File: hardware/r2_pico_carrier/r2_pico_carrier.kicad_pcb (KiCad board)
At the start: 2 copper layers, 80 x 72 mm, 63 parts, among them J1 5V in, J2 OLED SSD1306, SW1 display, U1 PCA9517A

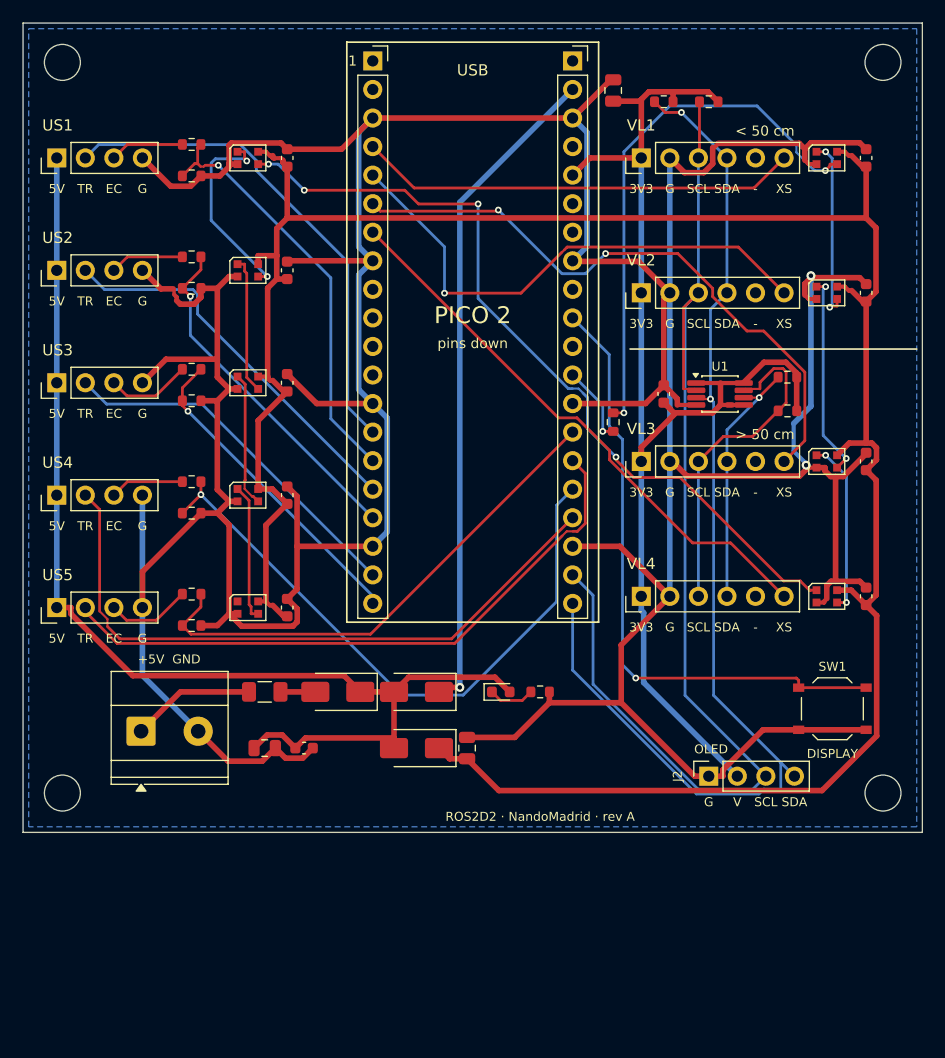
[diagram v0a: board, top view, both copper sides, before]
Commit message: Carrier board: PCA9517A port A (no offset) on the long cables; README warns about Pico orientation, terminal wiring with USB in, SW1 rotation
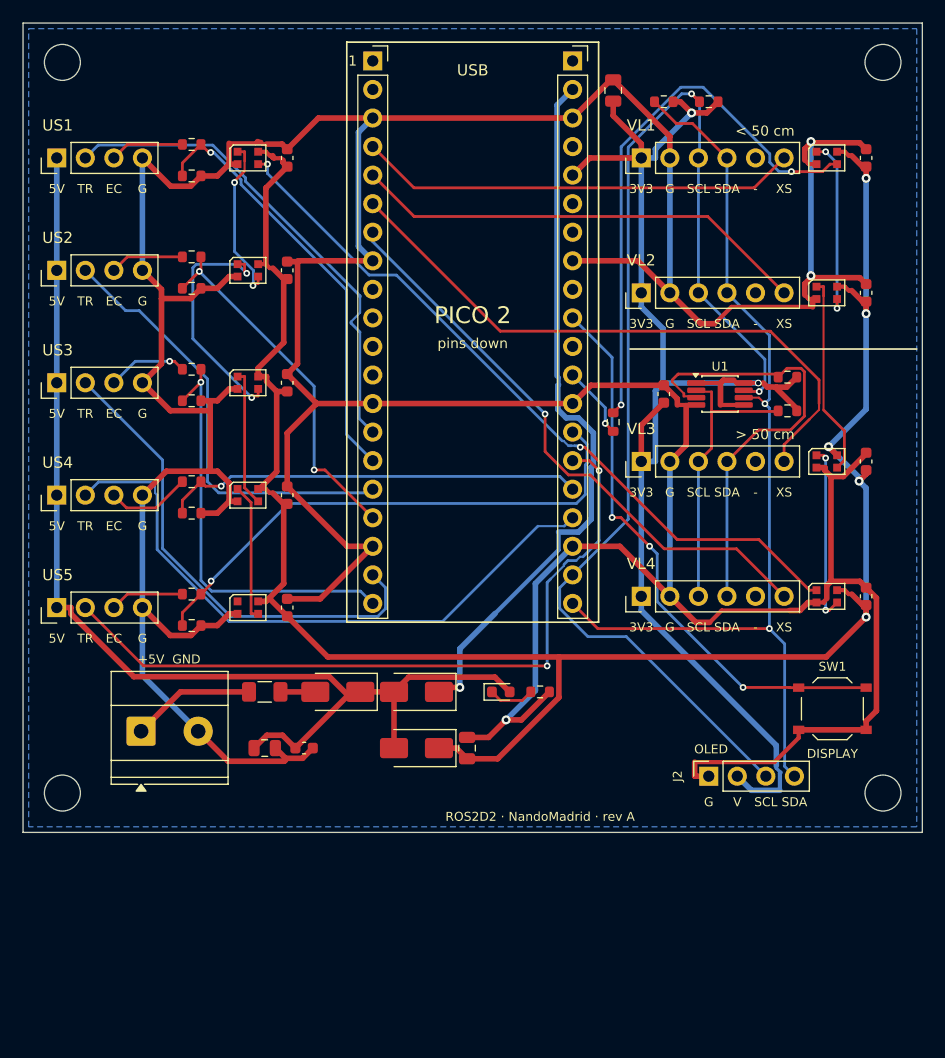
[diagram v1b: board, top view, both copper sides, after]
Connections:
- U1 pad 2: SCL -> SCL_L
- U1 pad 3: SDA -> SDA_L
- U1 pad 6: SDA_L -> SDA
- U1 pad 7: SCL_L -> SCL
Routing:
- net VLED: track 214.8 -> 181.8 mm, vias 0 -> 5
- net ECHO4_P: track 56.5 -> 37.5 mm
- net SDA_L: track 22.8 -> 40.1 mm, vias 1 -> 0
- net GND: track 470.4 -> 453.2 mm, vias 2 -> 3
- net +3V3: track 110.1 -> 124.0 mm, vias 0 -> 2
- net SDA: track 100.1 -> 86.9 mm
- net TRIG3: track 32.6 -> 43.7 mm
- net LED_D6: track 12.2 -> 21.8 mm, vias 0 -> 2
- net TRIG5: track 56.5 -> 65.8 mm, vias 0 -> 2
- net ECHO3_P: track 28.5 -> 37.2 mm
- net LED_D4: track 72.1 -> 65.9 mm, vias 4 -> 2
- net XSHUT2: track 46.7 -> 40.9 mm, vias 1 -> 0
- net BTN: track 55.6 -> 50.6 mm, vias 1 -> 3
- net TRIG2: track 34.7 -> 39.3 mm
- net VSYS: track 59.4 -> 63.8 mm
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
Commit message: Carrier board: OLED (HS96L03W2C03) fitted at the factory, lying flat; round Astromech Spain logo; 80 x 90 mm
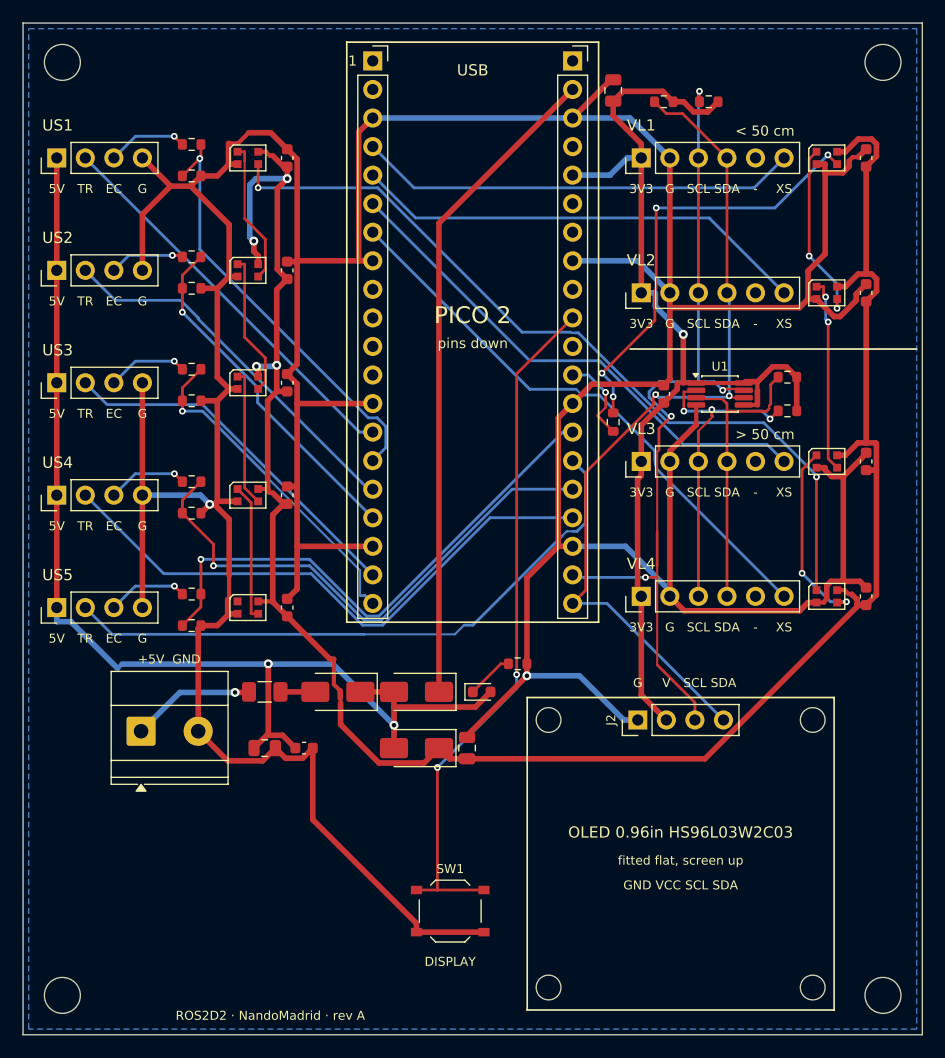
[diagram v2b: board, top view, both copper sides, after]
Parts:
- added H5: M2 OLED, MountingHole:MountingHole_2.2mm_M2, F.Cu at (46.8, 62.0)
- added H6: M2 OLED, MountingHole:MountingHole_2.2mm_M2, F.Cu at (70.2, 62.0)
- added H7: M2 OLED, MountingHole:MountingHole_2.2mm_M2, F.Cu at (46.8, 85.8)
- added H8: M2 OLED, MountingHole:MountingHole_2.2mm_M2, F.Cu at (70.2, 85.8)
- J2: value OLED SSD1306 -> OLED HS96L03W2C03; footprint Connector_PinSocket_2.54mm:PinSocket_1x04_P2.54mm_Vertical -> Connector_PinHeader_2.54mm:PinHeader_1x04_P2.54mm_Vertical
- moved SW1 38.5 mm to (38.0, 79.0)
- moved H3 18.0 mm to (3.50, 86.5)
- moved H4 18.0 mm to (76.5, 86.5)
- moved J2 8.05 mm to (54.7, 62.0)
- moved R1 3.20 mm to (44.0, 57.0)
- moved D4 1.70 mm to (40.8, 59.5)
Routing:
- net SCL: track 107.6 -> 75.7 mm, vias 2 -> 4
- net +3V3: track 124.0 -> 96.4 mm, vias 2 -> 1
- net SDA_L: track 40.1 -> 27.1 mm
- net BTN: track 50.6 -> 61.9 mm, vias 3 -> 2
- net TRIG3: track 43.7 -> 32.6 mm
- net ECHO4_P: track 37.5 -> 48.1 mm
- net TRIG5: track 65.8 -> 55.6 mm, vias 2 -> 0
- net LED_DIN: track 49.2 -> 39.0 mm, vias 2 -> 4
- net SDA: track 86.9 -> 77.2 mm
- net LED_D6: track 21.8 -> 12.8 mm, vias 2 -> 0
- net XSHUT3: track 54.7 -> 46.1 mm
- net TRIG1: track 44.0 -> 35.7 mm
- net ECHO3_P: track 37.2 -> 29.8 mm
- net LED_D4: track 65.9 -> 72.6 mm
- net VLED: track 181.8 -> 187.6 mm, vias 5 -> 4
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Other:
- board size 80 x 72 mm -> 80 x 90 mm
- board text added: "GND VCC SCL SDA"
- board text added: "OLED 0.96in HS96L03W2C03"
- board text added: "by NandoMadrid"
- board text added: "fitted flat, screen up"
- board text removed: "OLED"
- board text removed: "ROS2D2 · by NandoMadrid"

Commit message: Carrier board: in-stock Pico sockets (C2905423) and power LED (C2286, red); OLED plugs into a 4-pin socket (C2718488)
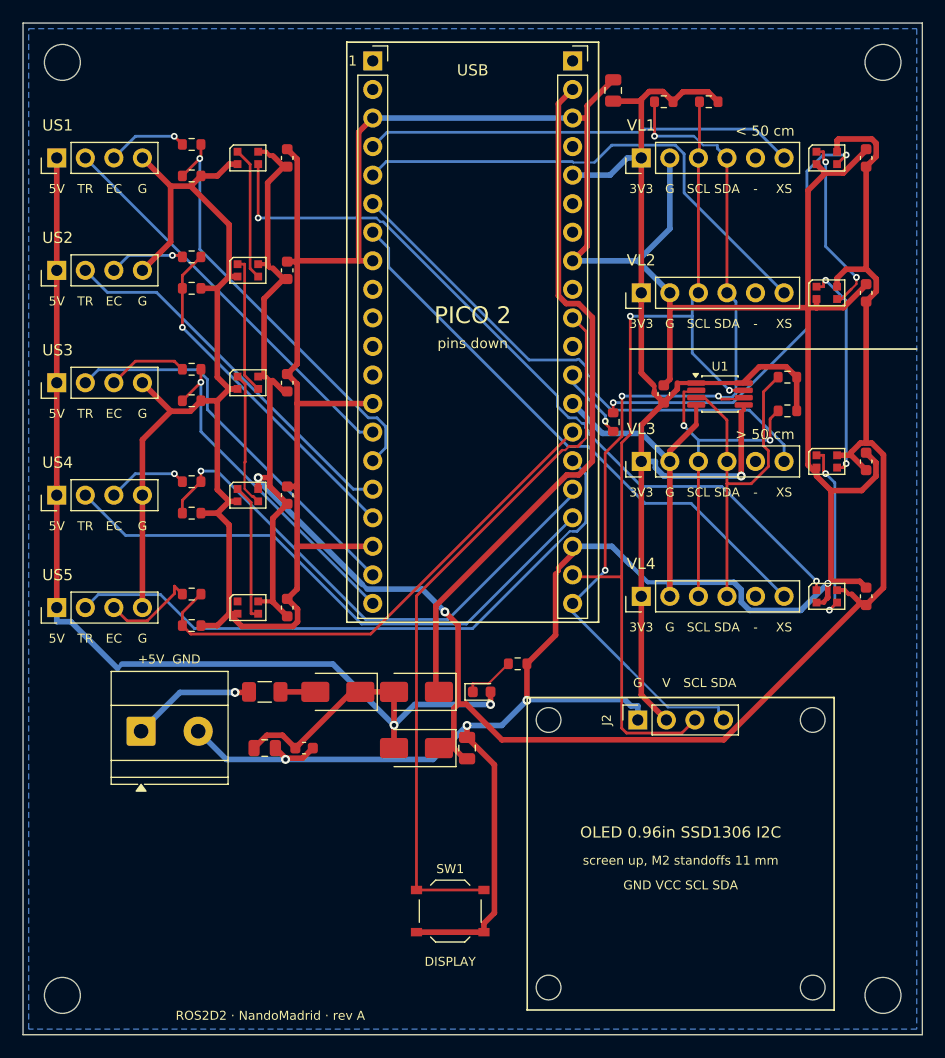
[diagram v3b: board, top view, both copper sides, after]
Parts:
- D4: value green -> red
- J2: value OLED HS96L03W2C03 -> OLED socket; footprint Connector_PinHeader_2.54mm:PinHeader_1x04_P2.54mm_Vertical -> Connector_PinSocket_2.54mm:PinSocket_1x04_P2.54mm_Vertical
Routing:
- net GND: track 451.6 -> 469.7 mm, vias 2 -> 4
- net +3V3: track 96.4 -> 108.3 mm
- net SCL: track 75.7 -> 82.7 mm, vias 4 -> 2
- net VLED: track 187.6 -> 194.1 mm, vias 4 -> 2
- net SDA: track 77.2 -> 83.3 mm, vias 2 -> 4
- net SDA_L: track 27.1 -> 32.2 mm
- net XSHUT2: track 40.9 -> 45.2 mm
- net VSYS: track 58.5 -> 62.5 mm
- net LED_D4: track 72.6 -> 69.5 mm
- net +5V: track 103.5 -> 106.3 mm
- net ECHO5_P: track 48.5 -> 46.0 mm, vias 1 -> 0
- net TRIG3: track 32.6 -> 35.2 mm
- net BTN: track 61.9 -> 64.3 mm, vias 2 -> 0
- net LED_D2: track 17.2 -> 19.4 mm
- net XSHUT3: track 46.1 -> 48.0 mm
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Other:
- board text added: "OLED 0.96in SSD1306 I2C"
- board text added: "screen up, M2 standoffs 11 mm"
- board text removed: "OLED 0.96in HS96L03W2C03"
- board text removed: "fitted flat, screen up"

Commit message: Carrier board: WS2812B-2020-V6 (in stock) for the diagnostic LEDs
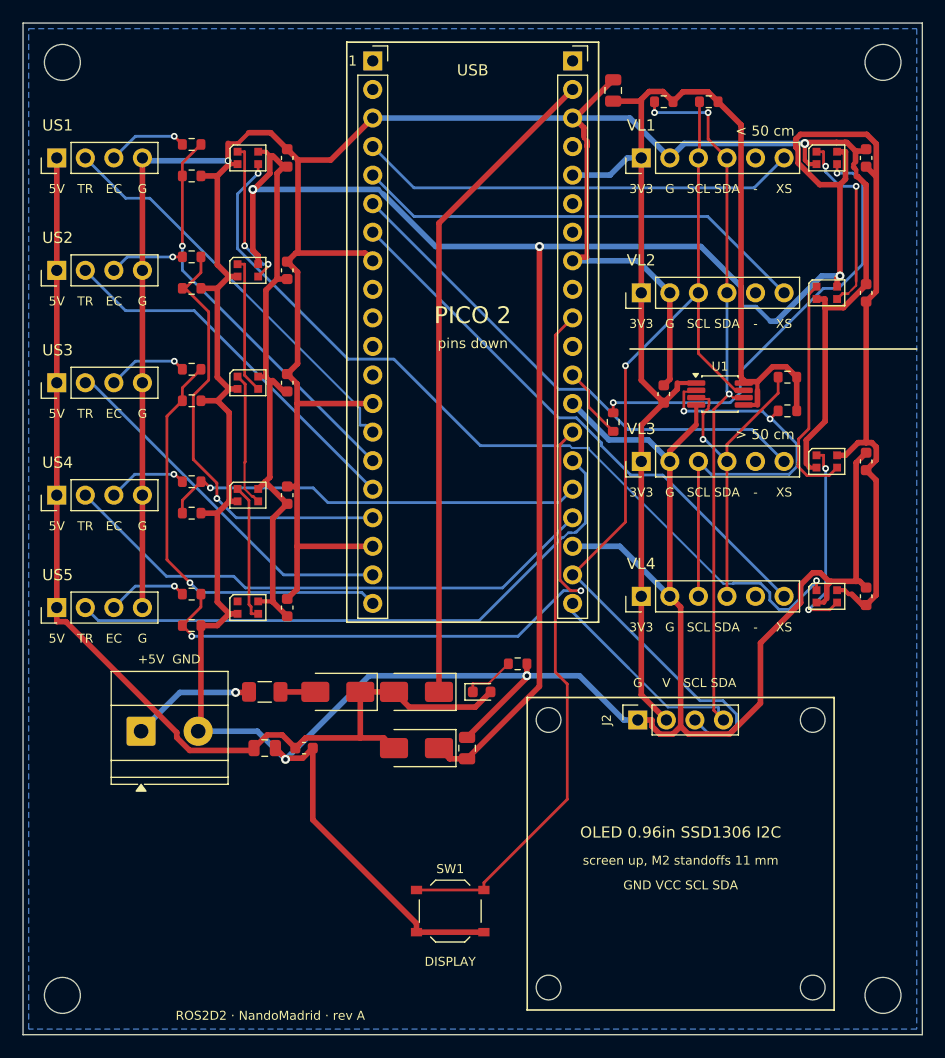
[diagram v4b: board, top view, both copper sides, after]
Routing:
- net VLED: track 194.1 -> 251.3 mm, vias 2 -> 3
- net GND: track 469.7 -> 496.2 mm
- net +5V: track 106.3 -> 94.9 mm, vias 2 -> 0
- net ECHO5_P: track 46.0 -> 57.0 mm, vias 0 -> 2
- net ECHO4_P: track 48.1 -> 37.8 mm
- net SCL_L: track 29.2 -> 38.7 mm
- net +3V3: track 108.3 -> 117.1 mm, vias 1 -> 0
- net ECHO3_P: track 29.5 -> 38.1 mm
- net ECHO2_P: track 30.9 -> 39.2 mm
- net LED_D4: track 69.5 -> 75.5 mm
- net XSHUT2: track 45.2 -> 40.9 mm
- net VSYS: track 62.5 -> 58.5 mm
- net BTN: track 64.3 -> 61.0 mm
- net SDA_L: track 32.2 -> 29.3 mm, vias 0 -> 1
- net TRIG4: track 52.0 -> 49.4 mm
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
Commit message: Carrier board: classic 5050 WS2812B (C2874885) for the diagnostic LEDs
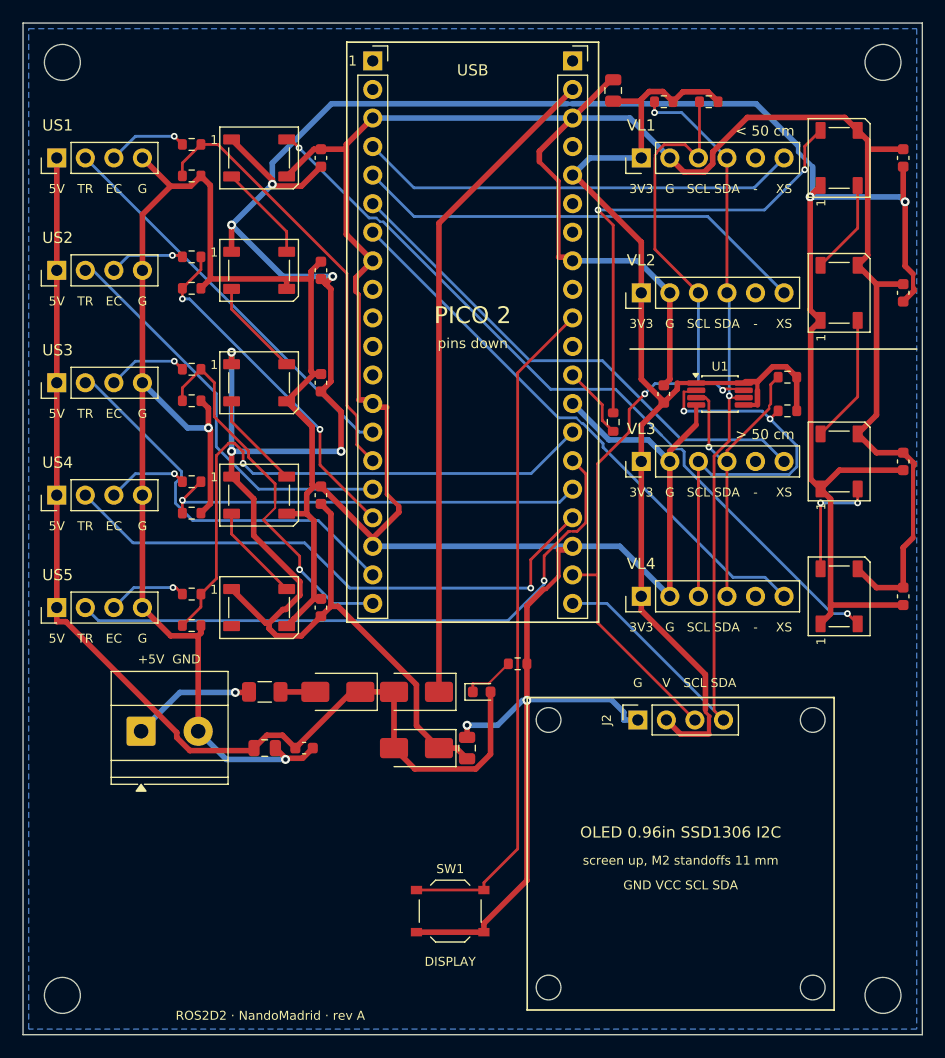
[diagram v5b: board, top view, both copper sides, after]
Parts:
- LED1, LED2, LED3, LED4, LED5, LED6, LED7, LED8, LED9: value WS2812B-2020 -> WS2812B; footprint LED_SMD:LED_WS2812B-2020_PLCC4_2.0x2.0mm -> LED_SMD:LED_WS2812B_PLCC4_5.0x5.0mm_P3.2mm
- moved C11 3.30 mm to (78.3, 12.0)
- moved C12 3.30 mm to (78.3, 24.0)
- moved C13 3.30 mm to (78.3, 39.0)
- moved C14 3.30 mm to (78.3, 51.0)
- moved C15 3.00 mm to (26.5, 12.0)
- moved C16 3.00 mm to (26.5, 22.0)
- moved C17 3.00 mm to (26.5, 32.0)
- moved C18 3.00 mm to (26.5, 42.0)
- moved C19 3.00 mm to (26.5, 52.0)
- moved LED1 1.10 mm to (72.6, 12.0), turned to 90 degrees
- moved LED2 1.10 mm to (72.6, 24.0), turned to 90 degrees
- moved LED3 1.10 mm to (72.6, 39.0), turned to 90 degrees
- moved LED4 1.10 mm to (72.6, 51.0), turned to 90 degrees
- moved LED5 1.00 mm to (21.0, 12.0)
- moved LED6 1.00 mm to (21.0, 22.0)
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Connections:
- LED1 pad 1: LED_D1 -> VLED
- LED1 pad 2: GND -> LED_D1
- LED1 pad 3: LED_DIN -> GND
- LED1 pad 4: VLED -> LED_DIN
- LED2 pad 1: LED_D2 -> VLED
- LED2 pad 2: GND -> LED_D2
- LED2 pad 3: LED_D1 -> GND
- LED2 pad 4: VLED -> LED_D1
- LED3 pad 1: LED_D3 -> VLED
- LED3 pad 2: GND -> LED_D3
- LED3 pad 3: LED_D2 -> GND
- LED3 pad 4: VLED -> LED_D2
- LED4 pad 1: LED_D4 -> VLED
- LED4 pad 2: GND -> LED_D4
- LED4 pad 3: LED_D3 -> GND
- LED4 pad 4: VLED -> LED_D3
- LED5 pad 1: LED_D5 -> VLED
- LED5 pad 2: GND -> LED_D5
- LED5 pad 3: LED_D4 -> GND
- LED5 pad 4: VLED -> LED_D4
- LED6 pad 1: LED_D6 -> VLED
- LED6 pad 2: GND -> LED_D6
- LED6 pad 3: LED_D5 -> GND
- LED6 pad 4: VLED -> LED_D5
- LED7 pad 1: LED_D7 -> VLED
- LED7 pad 2: GND -> LED_D7
- LED7 pad 3: LED_D6 -> GND
- LED7 pad 4: VLED -> LED_D6
- LED8 pad 1: LED_D8 -> VLED
- LED8 pad 2: GND -> LED_D8
- LED8 pad 3: LED_D7 -> GND
- LED8 pad 4: VLED -> LED_D7
- LED9 pad 1: unconnected-(LED9-DOUT-Pad1) -> VLED
- LED9 pad 2: GND -> unconnected-(LED9-DOUT-Pad2)
- LED9 pad 3: LED_D8 -> GND
- LED9 pad 4: VLED -> LED_D8
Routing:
- net GND: track 496.2 -> 473.4 mm
- net +3V3: track 117.1 -> 103.7 mm
- net VLED: track 251.3 -> 261.3 mm, vias 3 -> 8
- net LED_D2: track 20.8 -> 11.5 mm
- net LED_D1: track 16.8 -> 8.47 mm, vias 2 -> 0
- net ECHO2_P: track 39.2 -> 31.3 mm, vias 1 -> 2
- net LED_D3: track 17.9 -> 10.4 mm
- net LED_D4: track 75.5 -> 69.4 mm
- net ECHO5_P: track 57.0 -> 51.8 mm, vias 2 -> 1
- net +5V: track 94.9 -> 99.8 mm
- net SCL: track 82.7 -> 77.8 mm, vias 1 -> 2
- net ECHO3_P: track 38.1 -> 33.6 mm
- net LED_D5: track 13.2 -> 8.73 mm, vias 2 -> 0
- net LED_D6: track 12.2 -> 8.73 mm
- net LED_D8: track 12.2 -> 8.73 mm
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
